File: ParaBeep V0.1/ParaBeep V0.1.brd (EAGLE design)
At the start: 35.3 x 57.5 mm, 41 parts, among them J1 MICRO-SD_CARD_SOCKETPUSH-PUSH, U1 BQ25504RGTR, U3 TPS78330DDCRDDC5_TEX-L, U4 UBLOX_SAM_M8Q-0-10, U5 MS5803-14BA, U6 ATSAML10E16A-AFTTQFP32_MC_MCH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

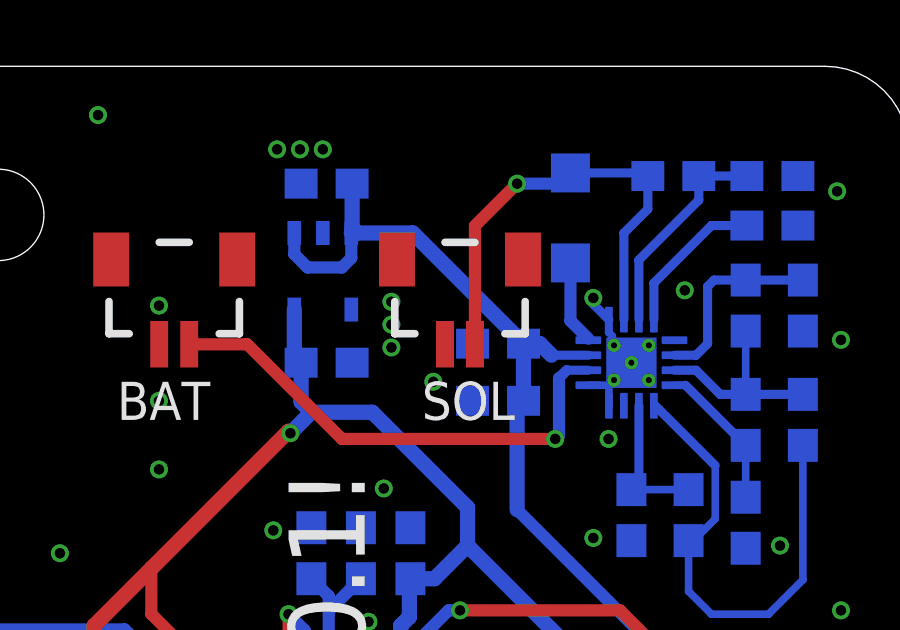
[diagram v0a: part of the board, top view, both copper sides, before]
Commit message: lots of parabeep code updates, gps started
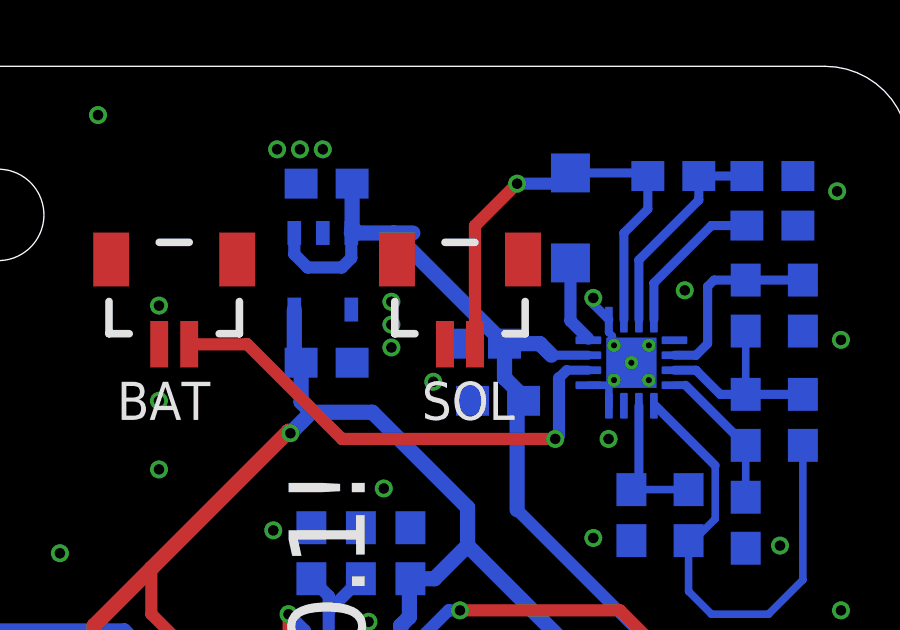
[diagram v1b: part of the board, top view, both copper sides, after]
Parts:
- R1, R3: value (none) -> 6.19M
- R10, R7: value (none) -> 4.42M
- R11: value (none) -> 15M
- R12: value (none) -> 3.32M
- R2: value (none) -> 542K
- R6: value (none) -> 3.83M
- R9: value (none) -> 5.65M
- moved C7 0.64 mm to (21.0, 48.3)
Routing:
- net VIN: track 30.7 -> 31.6 mm
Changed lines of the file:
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@@
 <attribute name="PROD_ID" value="CAP-08280" x="21.59" y="46.355" size="1.778" layer="28" rot="MR180" display="off"/>
 </element>
-<element name="C7" library="SparkFun-Capacitors" package="0603" value="0.1uF" x="21.59" y="48.26" smashed="yes" rot="MR180">
-<attribute name="NAME" x="21.59" y="47.498" size="0.6096" layer="26" font="vector" ratio="20" rot="MR180" align="bottom-center"/>
-<attribute name="PROD_ID" value="CAP-08604" x="21.59" y="48.26" size="1.778" layer="28" rot="MR180" display="off"/>
+<element name="C7" library="SparkFun-Capacitors" package="0603" value="0.1uF" x="20.955" y="48.26" smashed="yes" rot="MR180">
+<attribute name="NAME" x="20.955" y="47.498" size="0.6096" layer="26" font="vector" ratio="20" rot="MR180" align="bottom-center"/>
+<attribute name="PROD_ID" value="CAP-08604" x="20.955" y="48.26" size="1.778" layer="28" rot="MR180" display="off"/>
 </element>
 <element name="C8" library="SparkFun-Capacitors" package="0603" value="10nF" x="30.734" y="52.197" smashed="yes" rot="MR0">
@@
 <attribute name="PROD_ID" value="CAP-00867" x="30.734" y="52.197" size="1.778" layer="28" rot="MR0" display="off"/>
 </element>
-<element name="R1" library="SparkFun-Resistors" package="0603" value=" " x="27.94" y="42.545" smashed="yes" rot="MR270">
+<element name="R1" library="SparkFun-Resistors" package="0603" value="6.19M" x="27.94" y="42.545" smashed="yes" rot="MR270">
 <attribute name="NAME" x="27.813" y="40.005" size="0.6096" layer="26" font="vector" ratio="20" rot="MR270" align="bottom-center"/>
 <attribute name="PROD_ID" value=" " x="27.94" y="42.545" size="1.778" layer="28" rot="MR270" display="off"/>
 <attribute name="VALUE" x="28.702" y="42.545" size="0.6096" layer="28" font="vector" ratio="20" rot="MR270" align="top-center"/>
 </element>
-<element name="R2" library="SparkFun-Resistors" package="0603" value=" " x="31.75" y="45.72" smashed="yes" rot="MR90">
+<element name="R2" library="SparkFun-Resistors" package="0603" value="542K" x="31.75" y="45.72" smashed="yes" rot="MR90">
 <attribute name="NAME" x="32.512" y="45.72" size="0.6096" layer="26" font="vector" ratio="20" rot="MR90" align="bottom-center"/>
 <attribute name="PROD_ID" value=" " x="31.75" y="45.72" size="1.778" layer="28" rot="MR90" display="off"/>
 <attribute name="VALUE" x="30.988" y="45.72" size="0.6096" layer="28" font="vector" ratio="20" rot="MR90" align="top-center"/>
 </element>
-<element name="R3" library="SparkFun-Resistors" package="0603" value=" " x="29.845" y="45.72" smashed="yes" rot="MR270">
+<element name="R3" library="SparkFun-Resistors" package="0603" value="6.19M" x="29.845" y="45.72" smashed="yes" rot="MR270">
 <attribute name="NAME" x="29.083" y="45.72" size="0.6096" layer="26" font="vector" ratio="20" rot="MR270" align="bottom-center"/>
 <attribute name="PROD_ID" value=" " x="29.845" y="45.72" size="1.778" layer="28" rot="MR270" display="off"/>
 <attribute name="VALUE" x="30.607" y="45.72" size="0.6096" layer="28" font="vector" ratio="20" rot="MR270" align="top-center"/>
 </element>
-<element name="R6" library="SparkFun-Resistors" package="0603" value=" " x="29.845" y="42.291" smashed="yes" rot="MR270">
+<element name="R6" library="SparkFun-Resistors" package="0603" value="3.83M" x="29.845" y="42.291" smashed="yes" rot="MR270">
 <attribute name="NAME" x="30.353" y="39.751" size="0.6096" layer="26" font="vector" ratio="20" rot="MR270" align="bottom-center"/>
 <attribute name="PROD_ID" value=" " x="29.845" y="42.291" size="1.778" layer="28" rot="MR270" display="off"/>
 <attribute name="VALUE" x="30.607" y="42.291" size="0.6096" layer="28" font="vector" ratio="20" rot="MR270" align="top-center"/>
 </element>
-<element name="R7" library="SparkFun-Resistors" package="0603" value=" " x="31.75" y="49.53" smashed="yes" rot="MR270">
+<element name="R7" library="SparkFun-Resistors" package="0603" value="4.42M" x="31.75" y="49.53" smashed="yes" rot="MR270">
 <attribute name="NAME" x="32.893" y="49.53" size="0.6096" layer="26" font="vector" ratio="20" rot="MR270" align="bottom-center"/>
 <attribute name="PROD_ID" value=" " x="31.75" y="49.53" size="1.778" layer="28" rot="MR270" display="off"/>
 <attribute name="VALUE" x="32.512" y="49.53" size="0.6096" layer="28" font="vector" ratio="20" rot="MR270" align="top-center"/>
 </element>
-<element name="R9" library="SparkFun-Resistors" package="0603" value=" " x="29.845" y="49.53" smashed="yes" rot="MR90">
+<element name="R9" library="SparkFun-Resistors" package="0603" value="5.65M" x="29.845" y="49.53" smashed="yes" rot="MR90">
 <attribute name="NAME" x="28.702" y="49.53" size="0.6096" layer="26" font="vector" ratio="20" rot="MR90" align="bottom-center"/>
 <attribute name="PROD_ID" value=" " x="29.845" y="49.53" size="1.778" layer="28" rot="MR90" display="off"/>
 <attribute name="VALUE" x="29.083" y="49.53" size="0.6096" layer="28" font="vector" ratio="20" rot="MR90" align="top-center"/>
 </element>
-<element name="R10" library="SparkFun-Resistors" package="0603" value=" " x="27.432" y="53.848" smashed="yes" rot="MR180">
+<element name="R10" library="SparkFun-Resistors" package="0603" value="4.42M" x="27.432" y="53.848" smashed="yes" rot="MR180">
 <attribute name="NAME" x="27.432" y="55.626" size="0.6096" layer="26" font="vector" ratio="20" rot="MR180" align="bottom-center"/>
 <attribute name="PROD_ID" value=" " x="27.432" y="53.848" size="1.778" layer="28" rot="MR180" display="off"/>
 <attribute name="VALUE" x="27.432" y="54.61" size="0.6096" layer="28" font="vector" ratio="20" rot="MR180" align="top-center"/>
 </element>
-<element name="R11" library="SparkFun-Resistors" package="0603" value=" " x="30.734" y="53.848" smashed="yes" rot="MR180">
+<element name="R11" library="SparkFun-Resistors" package="0603" value="15M" x="30.734" y="53.848" smashed="yes" rot="MR180">
 <attribute name="NAME" x="30.607" y="55.245" size="0.6096" layer="26" font="vector" ratio="20" rot="MR180" align="bottom-center"/>
 <attribute name="PROD_ID" value=" " x="30.734" y="53.848" size="1.778" layer="28" rot="MR180" display="off"/>
 </element>
-<element name="R12" library="SparkFun-Resistors" package="0603" value=" " x="26.035" y="42.545" smashed="yes" rot="MR270">
+<element name="R12" library="SparkFun-Resistors" package="0603" value="3.32M" x="26.035" y="42.545" smashed="yes" rot="MR270">
 <attribute name="NAME" x="25.908" y="40.005" size="0.6096" layer="26" font="vector" ratio="20" rot="MR270" align="bottom-center"/>
 <attribute name="PROD_ID" value=" " x="26.035" y="42.545" size="1.778" layer="28" rot="MR270" display="off"/>
@@
 <wire x1="22.44" y1="46.482" x2="22.44" y2="46.355" width="0.3048" layer="16"/>
 <contactref element="JP1" pad="1"/>
-<wire x1="18.75065" y1="51.94935" x2="16.891" y2="51.94935" width="0.3048" layer="16"/>
+<wire x1="18.75065" y1="51.94935" x2="18.11565" y2="51.94935" width="0.3048" layer="16"/>
+<wire x1="18.11565" y1="51.94935" x2="16.891" y2="51.94935" width="0.3048" layer="16"/>
 <wire x1="16.891" y1="51.94935" x2="16.698" y2="51.94935" width="0.3048" layer="16"/>
 <wire x1="16.698" y1="51.94935" x2="16.698" y2="53.567" width="0.3048" layer="16"/>
@@
 <wire x1="16.725" y1="52.11535" x2="16.891" y2="51.94935" width="0.508" layer="16"/>
 <wire x1="16.698" y1="51.94935" x2="18.75065" y2="51.94935" width="0.508" layer="16"/>
-<wire x1="18.75065" y1="51.94935" x2="22.44" y2="48.26" width="0.508" layer="16"/>
-<wire x1="22.44" y1="48.26" x2="22.983" y2="48.26" width="0.508" layer="16"/>
+<wire x1="18.11565" y1="51.94935" x2="21.805" y2="48.26" width="0.508" layer="16"/>
+<wire x1="21.805" y1="48.26" x2="22.983" y2="48.26" width="0.508" layer="16"/>
 <wire x1="22.983" y1="48.26" x2="23.368" y2="47.875" width="0.508" layer="16"/>
-<wire x1="22.44" y1="48.26" x2="22.44" y2="46.482" width="0.508" layer="16"/>
+<wire x1="21.805" y1="48.26" x2="21.805" y2="47.117" width="0.508" layer="16"/>
+<wire x1="21.805" y1="47.117" x2="22.44" y2="46.482" width="0.508" layer="16"/>
 <wire x1="22.225" y1="42.7228" x2="26.67" y2="38.2778" width="0.4064" layer="16"/>
 <wire x1="22.44" y1="46.355" x2="22.225" y2="46.14" width="0.508" layer="16"/>
